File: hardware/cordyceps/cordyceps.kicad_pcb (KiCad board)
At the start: 4 copper layers, 24.6 x 29.9 mm, 23 parts, among them J1 KH-1.27PH180-2X5P-L7.2-SMT, SW1 TS-1187A-B-A-B, U1 nRF52833-QDxx, X1 32Mhz crystal, X2 32.768kHz crystal

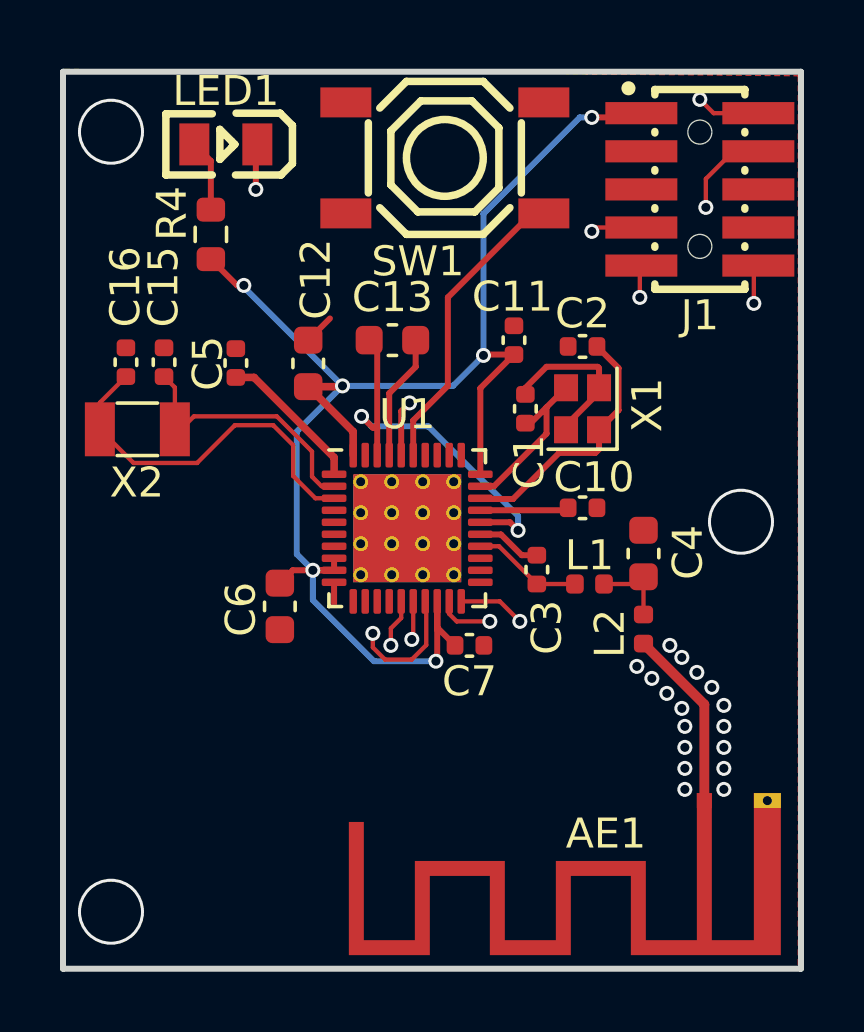
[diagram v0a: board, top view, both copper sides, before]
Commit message: Reposition some components to make the board even smaller
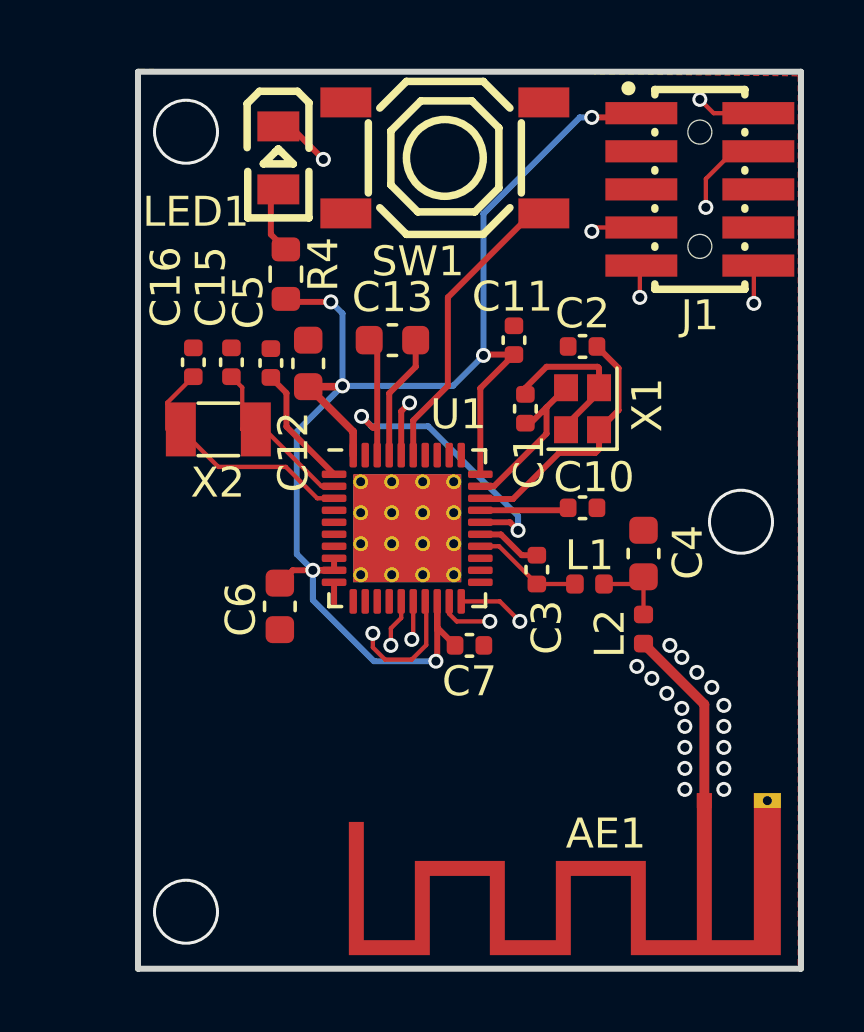
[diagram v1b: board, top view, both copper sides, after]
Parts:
- moved R4 2.83 mm to (118.0, 78.8)
- moved X2 2.70 mm to (115.8, 84.0)
- moved C15 2.25 mm to (116.2, 81.8)
- moved C16 2.25 mm to (114.9, 81.8)
- moved LED1 1.81 mm to (117.8, 75.0), turned to -90 degrees
- moved C5 1.17 mm to (117.5, 81.8)
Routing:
- net Net-(U1-XL2/P0.01): track 12.5 -> 8.18 mm
- net Net-(U1-XL1/P0.00): track 8.85 -> 5.50 mm
- net VDD: track 52.9 -> 51.2 mm
- net GND: track 14.1 -> 13.1 mm
- net Net-(U1-DEC1): track 4.94 -> 4.10 mm
- net Net-(LED1-K): track 12.6 -> 13.4 mm
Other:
- board size 24.6 x 29.9 mm -> 22.1 x 29.9 mm

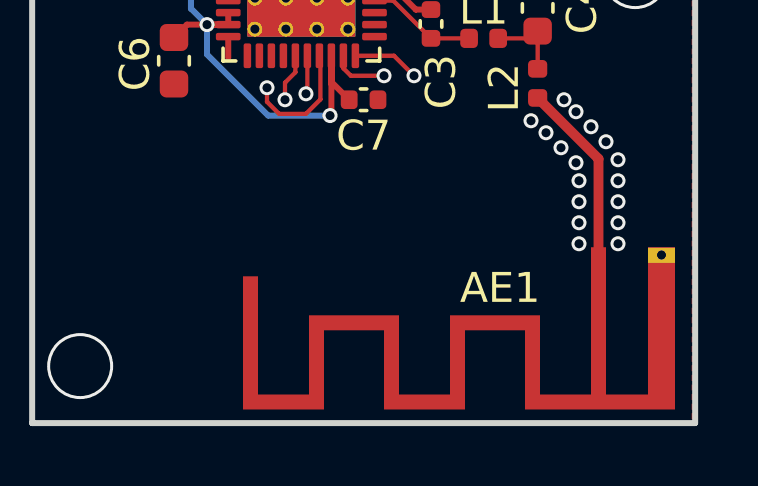
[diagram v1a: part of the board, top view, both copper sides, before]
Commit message: Add some stitching vias near the antenna
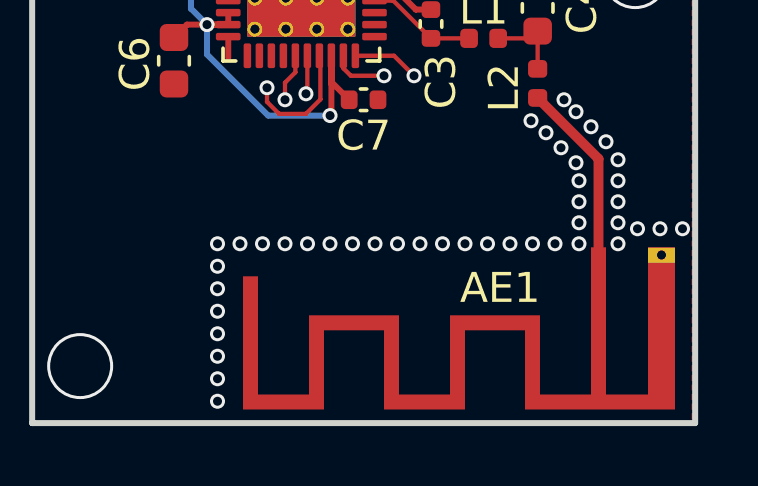
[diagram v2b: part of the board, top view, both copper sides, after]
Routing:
- net GND: vias 17 -> 43
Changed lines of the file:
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@@
 		(at 131.8 76 -90)
 		(property "Reference" "J1"
-			(at 4.2 0 180)
+			(at 4.2 0 360)
 			(layer "F.SilkS")
 			(effects
@@
 		)
 		(property "LCSC" "C22775"
-			(at 50.355 174.181 360)
+			(at 50.355 174.181 0)
 			(layer "F.Fab")
 			(hide yes)
@@
 	)
 	(via
+		(at 129 96)
+		(size 0.5)
+		(drill 0.3)
+		(layers "F.Cu" "B.Cu")
+		(free yes)
+		(net 3)
+	)
+	(via
+		(at 127.5 96)
+		(size 0.5)
+		(drill 0.3)
+		(layers "F.Cu" "B.Cu")
+		(free yes)
+		(net 3)
+	)
+	(via
 		(at 131.3 94.6)
 		(size 0.5)
@@
 	)
 	(via
+		(at 119.25 98.25)
+		(size 0.5)
+		(drill 0.3)
+		(layers "F.Cu" "B.Cu")
+		(free yes)
+		(net 3)
+	)
+	(via
 		(at 131.2 93.3)
 		(size 0.5)
@@
 	)
 	(via
+		(at 123.75 96)
+		(size 0.5)
+		(drill 0.3)
+		(layers "F.Cu" "B.Cu")
+		(free yes)
+		(net 3)
+	)
+	(via
 		(at 132.6 93.9)
 		(size 0.5)
@@
 	)
 	(via
+		(at 134 95.5)
+		(size 0.5)
+		(drill 0.3)
+		(layers "F.Cu" "B.Cu")
+		(free yes)
+		(net 3)
+	)
+	(via
+		(at 128.25 96)
+		(size 0.5)
+		(drill 0.3)
+		(layers "F.Cu" "B.Cu")
+		(free yes)
+		(net 3)
+	)
+	(via
+		(at 126.75 96)
+		(size 0.5)
+		(drill 0.3)
+		(layers "F.Cu" "B.Cu")
+		(free yes)
+		(net 3)
+	)
+	(via
+		(at 123 96)
+		(size 0.5)
+		(drill 0.3)
+		(layers "F.Cu" "B.Cu")
+		(free yes)
+		(net 3)
+	)
+	(via
+		(at 119.25 101.25)
+		(size 0.5)
+		(drill 0.3)
+		(layers "F.Cu" "B.Cu")
+		(free yes)
+		(net 3)
+	)
+	(via
 		(at 131.7 92.1)
 		(size 0.5)
@@
 	)
 	(via
+		(at 125.25 96)
+		(size 0.5)
+		(drill 0.3)
+		(layers "F.Cu" "B.Cu")
+		(free yes)
+		(net 3)
+	)
+	(via
 		(at 131.3 93.9)
 		(size 0.5)
@@
 	)
 	(via
+		(at 121.5 96)
+		(size 0.5)
+		(drill 0.3)
+		(layers "F.Cu" "B.Cu")
+		(free yes)
+		(net 3)
+	)
+	(via
+		(at 119.25 96.75)
+		(size 0.5)
+		(drill 0.3)
+		(layers "F.Cu" "B.Cu")
+		(free yes)
+		(net 3)
+	)
+	(via
+		(at 119.25 99)
+		(size 0.5)
+		(drill 0.3)
+		(layers "F.Cu" "B.Cu")
+		(free yes)
+		(net 3)
+	)
+	(via
+		(at 134.75 95.5)
+		(size 0.5)
+		(drill 0.3)
+		(layers "F.Cu" "B.Cu")
+		(free yes)
+		(net 3)
+	)
+	(via
+		(at 120 96)
+		(size 0.5)
+		(drill 0.3)
+		(layers "F.Cu" "B.Cu")
+		(free yes)
+		(net 3)
+	)
+	(via
 		(at 132.2 92.6)
 		(size 0.5)
@@
 	)
 	(via
+		(at 119.25 99.75)
+		(size 0.5)
+		(drill 0.3)
+		(layers "F.Cu" "B.Cu")
+		(free yes)
+		(net 3)
+	)
+	(via
+		(at 119.25 96)
+		(size 0.5)
+		(drill 0.3)
+		(layers "F.Cu" "B.Cu")
+		(free yes)
+		(net 3)
+	)
+	(via
+		(at 120.75 96)
+		(size 0.5)
+		(drill 0.3)
+		(layers "F.Cu" "B.Cu")
+		(free yes)
+		(net 3)
+	)
+	(via
+		(at 124.5 96)
+		(size 0.5)
+		(drill 0.3)
+		(layers "F.Cu" "B.Cu")
+		(free yes)
+		(net 3)
+	)
+	(via
 		(at 131.2 91.6)
 		(size 0.5)
@@
 	)
 	(via
+		(at 133.25 95.5)
+		(size 0.5)
+		(drill 0.3)
+		(layers "F.Cu" "B.Cu")
+		(free yes)
+		(net 3)
+	)
+	(via
+		(at 129.75 96)
+		(size 0.5)
+		(drill 0.3)
+		(layers "F.Cu" "B.Cu")
+		(free yes)
+		(net 3)
+	)
+	(via
 		(at 130.7 92.8)
 		(size 0.5)
@@
 	)
 	(via
+		(at 119.25 100.5)
+		(size 0.5)
+		(drill 0.3)
+		(layers "F.Cu" "B.Cu")
+		(free yes)
+		(net 3)
+	)
+	(via
 		(at 130.2 92.3)
 		(size 0.5)
@@
 	)
 	(via
+		(at 119.25 97.5)
+		(size 0.5)
+		(drill 0.3)
+		(layers "F.Cu" "B.Cu")
+		(free yes)
+		(net 3)
+	)
+	(via
+		(at 130.5 96)
+		(size 0.5)
+		(drill 0.3)
+		(layers "F.Cu" "B.Cu")
+		(free yes)
+		(net 3)
+	)
+	(via
 		(at 132.6 93.2)
 		(size 0.5)
 		(drill 0.3)
+		(layers "F.Cu" "B.Cu")
+		(free yes)
+		(net 3)
+	)
+	(via
+		(at 122.25 96)
+		(size 0.5)
+		(drill 0.3)
+		(layers "F.Cu" "B.Cu")
+		(free yes)
+		(net 3)
+	)
+	(via
+		(at 126 96)
+		(size 0.5)
+		(drill 0.3)
